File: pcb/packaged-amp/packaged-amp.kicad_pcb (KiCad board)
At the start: 4 copper layers, 70 x 86 mm, 105 parts, among them J2 RFShield_TwoPieces, J7 Conn_Coaxial, J8 USB_B, Q1 MMBT3906, Q2 MMBT3904, U1 TLV2172, U2 OPA2822, U3 LMR62014XMF, U4 L78L06_SOT89, U5 L79L05_SOT89

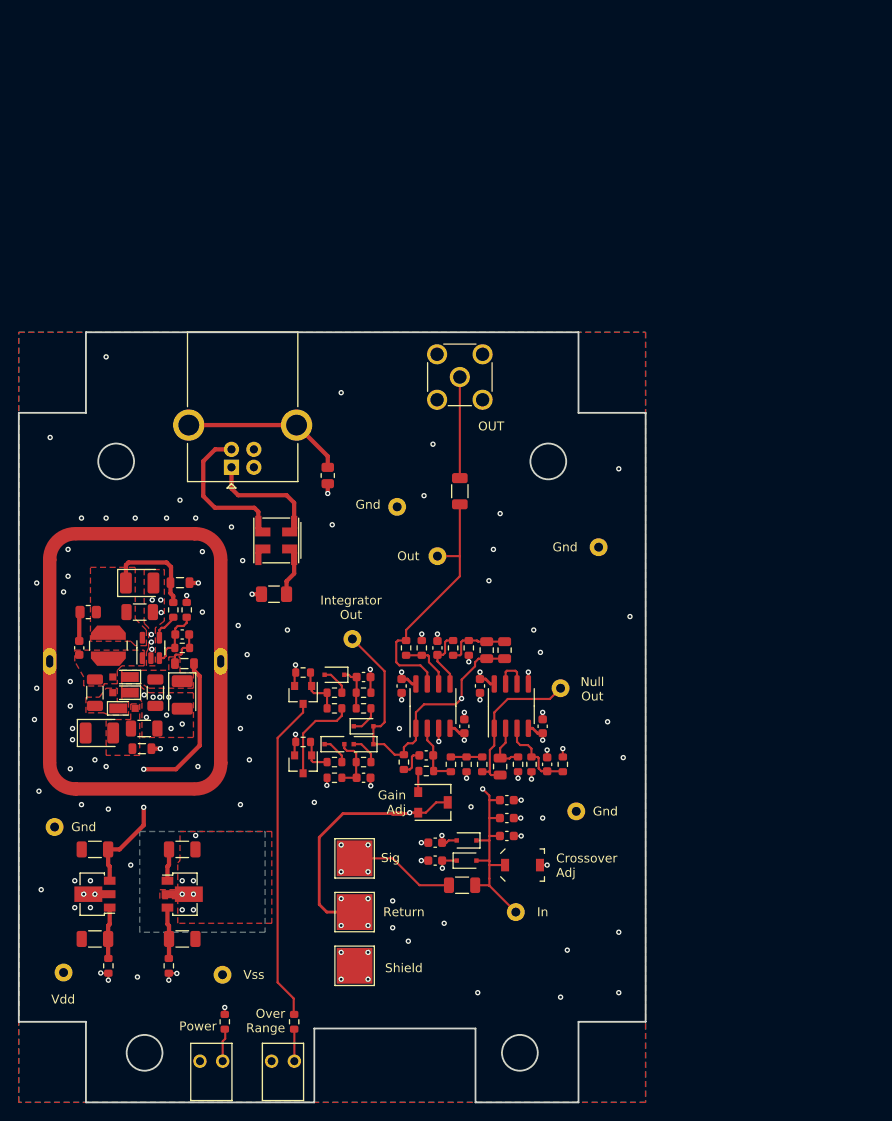
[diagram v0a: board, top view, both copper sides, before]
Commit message: finished design of packaged amp
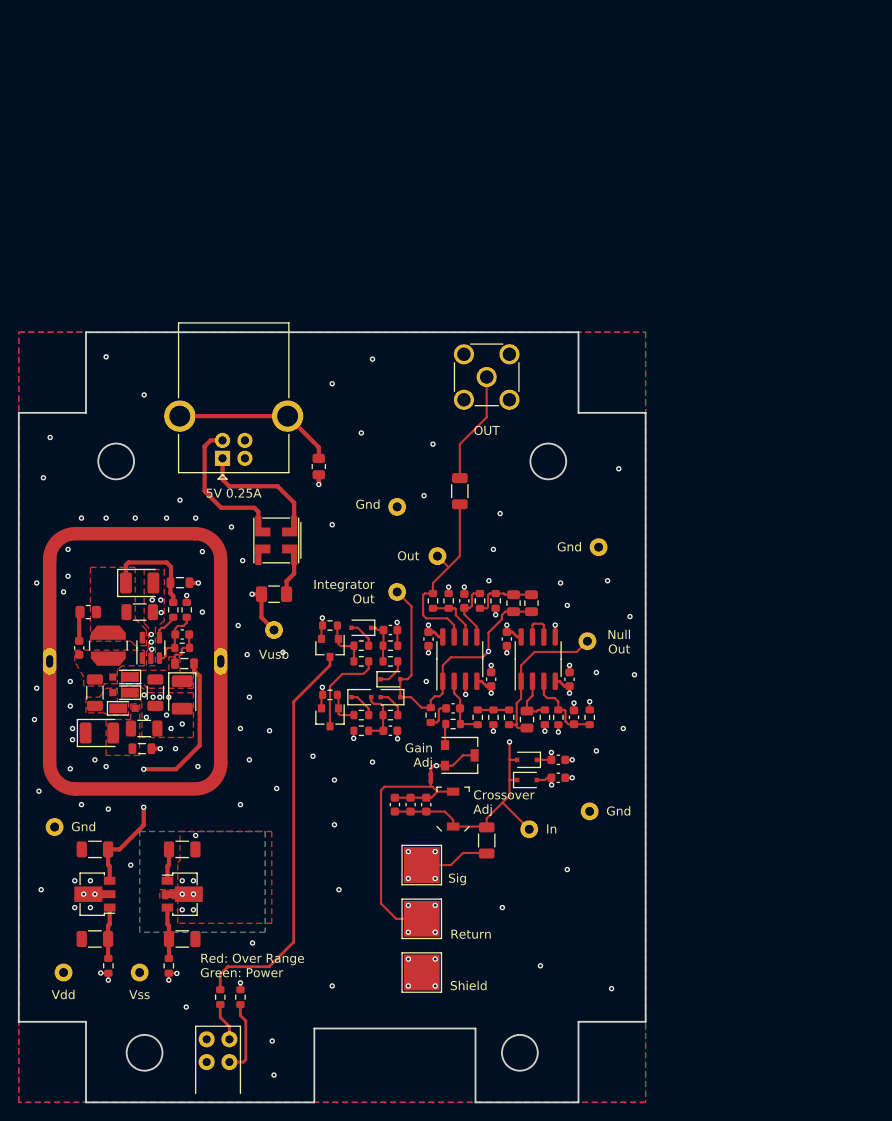
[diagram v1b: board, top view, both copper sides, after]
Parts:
- removed D11: LED, wbraun_smd:LED-T1-RIGHT-ANGLE_4.6x4.4mm
- added TP14: TestPoint, wbraun_smd:THM_MINI, F.Cu at (66.0, 129.8)
- D10: value LED -> LED_Dual_KAKA; footprint wbraun_smd:LED-T1-RIGHT-ANGLE_4.6x4.4mm -> wbraun_smd:LED_WP934MD
- moved C7 17.8 mm to (97.8, 144.2)
- moved C8 15.5 mm to (97.8, 146.2), turned to 180 degrees
- moved D1 13.1 mm to (94.2, 144.2), turned to 180 degrees
- moved C1 13.0 mm to (79.5, 149.2), turned to 90 degrees
- moved C10 10.9 mm to (81.2, 149.2), turned to 90 degrees
- moved C11 9.96 mm to (86.0, 149.8), turned to 90 degrees
- moved D2 9.55 mm to (94.2, 146.5), turned to 0 degrees
- moved TP1 9.37 mm to (94.5, 152.0)
- moved TP10 9.25 mm to (51.0, 168.0)
- moved C9 9.01 mm to (83.0, 149.2), turned to 90 degrees
- moved R28 8.70 mm to (60.0, 170.8)
- moved TP11 7.54 mm to (82.5, 156.0)
- moved TP12 7.54 mm to (82.5, 162.0)
- moved TP13 7.54 mm to (82.5, 168.0)
- moved D10 7.25 mm to (59.8, 178.0), turned to 0 degrees
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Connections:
- C1 pad 2: GND -> /return_kelvin
- C10 pad 2: GND -> /return_kelvin
- C11 pad 2: GND -> /return_kelvin
- C7 pad 1: VDD -> GND
- C7 pad 2: GND -> VDD
- C9 pad 2: GND -> /return_kelvin
- NT1 pad 1: Net-(NT1-Pad1) -> /return_kelvin
- R30 pad 2: Net-(D11-Pad1) -> Net-(R30-Pad2)
- TP12 pad 1: Net-(NT1-Pad1) -> /return_kelvin
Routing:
- net /return_kelvin: track 0.00 -> 31.9 mm, vias 0 -> 4
- net Net-(NT1-Pad1): track 21.1 -> 0.00 mm, vias 4 -> 0
- net Net-(R30-Pad2): track 0.00 -> 8.36 mm
- net Net-(Q2-Pad3): track 36.6 -> 44.9 mm
- net Net-(R12-Pad1): track 28.9 -> 21.6 mm
- net Net-(F1-Pad2): track 8.57 -> 13.2 mm
- net Net-(R1-Pad1): track 11.8 -> 7.84 mm
- net Net-(D11-Pad1): track 3.71 -> 0.00 mm
- net Net-(C1-Pad1): track 34.3 -> 37.1 mm
- net GND: track 25.7 -> 23.0 mm, vias 111 -> 117
- net Net-(J8-Pad1): track 12.2 -> 13.6 mm
- net Net-(J7-Pad1): track 11.3 -> 12.5 mm
- net /int_out: track 50.7 -> 49.8 mm
- net Net-(R28-Pad2): track 3.58 -> 4.31 mm
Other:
- board text added: "5V 0.25A"
- board text added: "Red: Over Range Green: Power"
- board text added: "Vusb"
- board text removed: "Over Range"
- board text removed: "Power"

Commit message: design sent to fab
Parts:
- added D11: SMAJ6.0A-13-F, Diode_SMD:D_SMA, F.Cu at (65.5, 131.0)
- added E1: SparkGap, wbraun_smd:Spark_Gap, F.Cu at (91.2, 154.0)
- added E2: SparkGap, wbraun_smd:Spark_Gap, F.Cu at (73.2, 147.8)
- added GD1: GDT_2Pin, wbraun_smd:GDT_1812, F.Cu at (92.2, 119.5)
- added NT2: NetTie_2, NetTie:NetTie-2_SMD_Pad0.5mm, F.Cu at (89.2, 169.0)
- moved TP14 10.0 mm to (65.2, 139.8)
- moved TP6 6.71 mm to (104.2, 144.0)
- moved R1 3.26 mm to (89.5, 150.0)
- moved TP11 2.50 mm to (80.5, 157.5)
- moved TP12 2.50 mm to (80.5, 163.5)
- moved TP13 2.50 mm to (80.5, 169.5)
- moved TP1 2.37 mm to (95.2, 149.8)
- moved J8 1.00 mm to (60.2, 109.6)
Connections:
- TP13 pad 1: GND -> Net-(NT2-Pad1)
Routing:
- net /return_kelvin: track 31.9 -> 45.7 mm
- net Net-(D11-Pad1): track 13.2 -> 26.6 mm
- net Net-(NT2-Pad1): track 0.00 -> 13.1 mm, vias 0 -> 4
- net Net-(E1-Pad2): track 7.84 -> 20.3 mm
- net Net-(GD1-Pad1): track 21.6 -> 28.2 mm
- net Net-(J8-Pad5): track 18.2 -> 20.7 mm
- net GND: track 23.0 -> 25.0 mm, vias 117 -> 132
- net Net-(J8-Pad4): track 15.4 -> 16.4 mm
- net Net-(J8-Pad1): track 13.6 -> 14.6 mm
- net Net-(C1-Pad1): track 37.1 -> 38.1 mm
- net Net-(Q2-Pad3): track 44.9 -> 45.8 mm
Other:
- outline, holes or cut-outs redrawn
- board text added: "Designed to fit hammond 1593BBBK enclosure"
- board text added: "JLCJLCJLCJLC"
- board text added: "Rogowski Coil Amplifier V1.0"
- board text removed: "OUT"

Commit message: next design revision
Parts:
- removed C18: 47n, Capacitor_SMD:C_0805_2012Metric
- removed C24, C26, C32: 47u, Capacitor_Tantalum_SMD:CP_EIA-3528-15_AVX-H
- removed C33, C34: C, Capacitor_SMD:C_0603_1608Metric
- removed C8: 0.47u, Capacitor_SMD:C_0603_1608Metric
- removed D10: LED_Dual_KAKA, wbraun_smd:LED_WP934MD
- removed D7: 1N4148, Diode_SMD:D_SOD-323F
- removed D8, D9: MM3Z7V5B, Diode_SMD:D_SOD-323F
- removed NT2: NetTie_2, NetTie:NetTie-2_SMD_Pad0.5mm
- removed Q1: MMBT3906, wbraun_smd:SOT-23
- removed Q2: MMBT3904, wbraun_smd:SOT-23
- removed R22, R23, R27: 47k, Resistor_SMD:R_0603_1608Metric
- removed R24, R29: 22k, Resistor_SMD:R_0603_1608Metric
- removed R26: 1M, Resistor_SMD:R_0603_1608Metric
- removed R28, R30: 4.7k, Resistor_SMD:R_0603_1608Metric
- removed R31, R32: 0, Resistor_SMD:R_0603_1608Metric
- removed TP1, TP10, TP2, TP3, TP5, TP7, TP8, TP9: TestPoint, wbraun_smd:THM_MINI
- removed TP13: TestPoint, TestPoint:TestPoint_Pad_4.0x4.0mm
- added C2: 10u, Capacitor_SMD:C_1206_3216Metric, F.Cu at (92.2, 105.0)
- added C3: 10u, Capacitor_SMD:C_1206_3216Metric, F.Cu at (83.8, 109.5)
- added C4: DNP, Capacitor_SMD:C_0603_1608Metric, F.Cu at (112.5, 98.8)
- added G***: LOGO, wbraun_smd:Beefield_logo, F.Cu at (97.8, 159.2)
- added J1: ECT81800C036, wbraun_smd:Shield_Clip_ECT81800C036, F.Cu at (88.0, 90.5)
- added J3: ECT81800C036, wbraun_smd:Shield_Clip_ECT81800C036, F.Cu at (88.0, 115.5)
- added J4: ECT81800C036, wbraun_smd:Shield_Clip_ECT81800C036, F.Cu at (98.0, 103.0)
- C10: value 22p -> DNP
- C11: value 8-40p -> 12-60p; footprint Capacitor_SMD:C_Trimmer_Voltronics_JZ -> wbraun_smd:C_Trimmer_GKG_6mm
- C15: footprint Capacitor_SMD:C_0805_2012Metric -> Capacitor_SMD:C_1206_3216Metric
- C17: value 47n -> DNP; footprint Capacitor_SMD:C_0805_2012Metric -> Capacitor_SMD:C_0603_1608Metric
- C19: value 22p -> 10p
- C22: value 470p -> 330p
- C7: value 0.47u -> 10u; footprint Capacitor_SMD:C_0603_1608Metric -> Capacitor_SMD:C_1206_3216Metric
- C9: value 150p -> 100p
- D11: value SMAJ6.0A-13-F -> P6SMB6.8CA/TR13; footprint Diode_SMD:D_SMA -> Diode_SMD:D_SMB
- D3, D4, D5: value PD3S140-7 -> BAT760-7; footprint wbraun_smd:D_POWERDI323 -> Diode_SMD:D_SOD-323
- D6: value 1N4148 -> LTST-S220KGKT; footprint Diode_SMD:D_SOD-323F -> wbraun_smd:LED-T1-RIGHT-ANGLE_4.6x4.4mm
- J2: value RFShield_TwoPieces -> ECT81800C036; footprint wbraun_smd:Masach_Tech_MS288-10F -> wbraun_smd:Shield_Clip_ECT81800C036
- L2: value L_Ferrite_Coupled -> DLW5BTM142SQ2L
- R1: footprint Resistor_SMD:R_1206_3216Metric -> Resistor_SMD:R_0603_1608Metric
- R10: value 220 -> 470
- R11, R12: value 2k -> 470
- R13: value 47 -> 100
- R15, R18: value 75k -> 82k
- R16: value 13.3k -> 13k
- R19: value R -> DNP
- R2: value 4.7k -> 22k
- R20: value 2k -> DNP
- R21: value 2k -> 100; footprint Resistor_SMD:R_0603_1608Metric -> Resistor_SMD:R_1206_3216Metric
- R25: value 1M -> 4.7k
- R3: value 10k -> 8.2k
- R4, R7: value 47k -> 22k
- R6: value 22k -> DNP
- R8: value 2k -> 10k
- R9: value 10k -> 2k
- RV1: footprint wbraun_smd:TRIMMER_PVG3A -> Potentiometer_SMD:Potentiometer_Bourns_3314G_Vertical
- U4: value L78L06_SOT89 -> MC78L06F-TP
- U5: value L79L05_SOT89 -> MC79L06F-TP
- moved TP4 112.7 mm to (126.2, 77.5)
- moved R20 63.4 mm to (114.5, 86.8), turned to 90 degrees
- moved TP14 62.3 mm to (79.2, 79.0)
- moved R21 60.8 mm to (110.5, 81.2), turned to -90 degrees
- moved C11 57.8 mm to (124.0, 106.2), turned to 180 degrees
- moved D2 56.6 mm to (125.8, 99.5)
- moved D1 56.4 mm to (125.8, 97.5)
- moved C30 56.3 mm to (87.8, 126.5)
- moved U4 55.3 mm to (87.5, 122.8)
- moved C15 54.9 mm to (105.2, 86.0)
- moved C28 54.6 mm to (87.8, 119.0)
- moved C16 54.0 mm to (111.0, 86.8), turned to -90 degrees
- moved R8 54.0 mm to (112.8, 86.8), turned to 90 degrees
- moved R4 53.9 mm to (103.2, 86.8)
- moved C31 53.7 mm to (94.0, 126.5)
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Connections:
- net Net-(C14-Pad1) renamed /int_fb
- C16 pad 1: Net-(C16-Pad1) -> GND
- C16 pad 2: GND -> Net-(C16-Pad2)
- C17 pad 1: /int_out -> /out
- C30 pad 1: Net-(C30-Pad1) -> VDD
- C31 pad 2: Net-(C31-Pad2) -> VSS
- C7 pad 1: GND -> /VBUS
- C7 pad 2: VDD -> GND
- D6 pad 1: /int_out -> VSS
- J7 pad 1: Net-(J7-Pad1) -> Net-(GD1-Pad1)
- R10 pad 2: Net-(C17-Pad2) -> /int_out
- R12 pad 1: Net-(GD1-Pad1) -> /out
- R13 pad 1: Net-(J7-Pad1) -> Net-(GD1-Pad1)
- R13 pad 2: Net-(GD1-Pad1) -> /out
- R20 pad 1: Net-(D6-Pad2) -> Net-(C17-Pad2)
- R20 pad 2: Net-(C33-Pad1) -> GND
- R21 pad 1: Net-(D7-Pad1) -> Net-(GD1-Pad1)
- R21 pad 2: Net-(C34-Pad1) -> /out
- R25 pad 1: Net-(Q1-Pad1) -> Net-(D6-Pad2)
- R6 pad 1: Net-(C15-Pad2) -> Net-(C4-Pad2)
- R7 pad 1: Net-(C16-Pad1) -> Net-(C15-Pad2)
- R7 pad 2: /int_out -> GND
- R8 pad 1: GND -> Net-(C16-Pad2)
- R8 pad 2: Net-(C16-Pad1) -> /out
- R9 pad 2: Net-(C17-Pad2) -> Net-(C16-Pad2)
- RV1 pad 1: Net-(R5-Pad1) -> GND
- RV1 pad 3: GND -> Net-(R5-Pad1)
- U1 pad 1: Net-(C15-Pad1) -> Net-(U1-Pad1)
- U1 pad 2: Net-(C15-Pad2) -> Net-(U1-Pad1)
- U1 pad 3: Net-(C16-Pad1) -> GND
- U1 pad 5: GND -> Net-(C16-Pad2)
- U1 pad 6: Net-(U1-Pad6) -> Net-(C15-Pad2)
- U1 pad 7: Net-(U1-Pad6) -> Net-(C15-Pad1)
- U2 pad 7: Net-(GD1-Pad1) -> /out
- U4 pad 1: Net-(C30-Pad1) -> VDD
- U5 pad 3: Net-(C31-Pad2) -> VSS
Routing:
- net Net-(Q2-Pad3): track 45.8 -> 0.00 mm
- net /int_out: track 49.8 -> 14.6 mm, vias 2 -> 0
- net Net-(R2-Pad2): track 3.50 -> 33.0 mm, vias 0 -> 2
- net /out: track 0.00 -> 16.8 mm
- net VSS: track 15.2 -> 30.7 mm, vias 8 -> 4
- net Net-(NT2-Pad1): track 13.1 -> 0.00 mm, vias 4 -> 0
- net Net-(E1-Pad2): track 20.3 -> 33.1 mm
- net Net-(J8-Pad4): track 16.4 -> 29.0 mm
- net Net-(J7-Pad1): track 12.5 -> 0.00 mm
- net Net-(J8-Pad1): track 14.6 -> 27.0 mm
- net Net-(C15-Pad1): track 17.7 -> 5.74 mm
- net Net-(Q1-Pad3): track 10.4 -> 0.00 mm
- net /return_kelvin: track 45.7 -> 56.1 mm
- net Net-(C16-Pad1): track 9.22 -> 0.00 mm
- net Net-(D10-Pad3): track 8.36 -> 0.00 mm
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- added copper zone on B.Cu, net GND
- added copper zone on In2.Cu, net GND
- added copper zone on In2.Cu, net VDD
- removed copper zone on B.Cu, net VDD
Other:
- board size 70 x 86 mm -> 56.6 x 82.7 mm
- board text removed: "5V 0.25A"
- board text removed: "Crossover Adj"
- board text removed: "Designed to fit hammond 1593BBBK enclosure"
- board text removed: "Gain Adj"
- board text removed: "In"
- board text removed: "Integrator Out"
- board text removed: "Null Out"
- board text removed: "Out"
- board text removed: "Red: Over Range Green: Power"
- board text removed: "Return"
- board text removed: "Shield"
- board text removed: "Sig"
- board text removed: "Vdd"
- board text removed: "Vss"
- board text removed: "Vusb"

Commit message: design revision
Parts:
- removed FB5: FerriteBead_Small, Inductor_SMD:L_0805_2012Metric
- removed G***: LOGO, wbraun_smd:Beefield_logo
- removed R19: DNP, Resistor_SMD:R_0805_2012Metric
- removed R20: DNP, Resistor_SMD:R_0603_1608Metric
- removed R21: 100, Resistor_SMD:R_1206_3216Metric
- removed TP14: TestPoint, wbraun_smd:THM_MINI
- added C18: 0.47u, Capacitor_SMD:C_0603_1608Metric, F.Cu at (84.8, 79.5)
- added C24: 10u, Capacitor_SMD:C_1206_3216Metric, F.Cu at (89.2, 85.2)
- added C8: 0.47u, Capacitor_SMD:C_0603_1608Metric, F.Cu at (84.8, 71.0)
- added H1: MountingHole, wbraun_smd:beefield_logo_small, F.Cu at (125.2, 141.6)
- added L3: 6.8u, Inductor_SMD:L_1210_3225Metric, F.Cu at (86.0, 85.2)
- added U6: B0505S-1WR3, wbraun_smd:Converter_DCDC_1W_Isolated_Short, F.Cu at (77.6, 71.0)
- C17: value DNP -> 1n; footprint Capacitor_SMD:C_0603_1608Metric -> Capacitor_SMD:C_1206_3216Metric
- C4: value DNP -> 10u; footprint Capacitor_SMD:C_0603_1608Metric -> Capacitor_SMD:C_1206_3216Metric
- D6: value LTST-S220KGKT -> WP934CB/GD
- L2: value DLW5BTM142SQ2L -> 6.8u; footprint wbraun_smd:L_CommonModeChoke_Murata_DLW5BTM -> Inductor_SMD:L_1210_3225Metric
- R13: value 100 -> 47
- R6: value DNP -> 47
- moved C4 43.1 mm to (84.2, 66.2), turned to 0 degrees
- moved C17 33.1 mm to (85.2, 75.2)
- moved TP6 22.5 mm to (129.2, 119.0)
- moved D11 17.0 mm to (89.0, 68.2), turned to 90 degrees
- moved TP4 15.2 mm to (114.0, 68.5)
- moved R6 14.5 mm to (125.2, 98.8)
- moved GD1 14.1 mm to (125.8, 76.5), turned to 0 degrees
- moved R13 10.8 mm to (123.5, 81.5)
- moved F1 7.91 mm to (89.0, 73.2), turned to 180 degrees
- moved L2 7.62 mm to (79.5, 66.2), turned to 180 degrees
- moved R25 6.77 mm to (84.0, 130.8), turned to 0 degrees
- moved D6 5.11 mm to (84.5, 136.9)
- moved C1 2.25 mm to (115.0, 107.8)
- moved C10 2.25 mm to (116.8, 107.8)
- moved C11 2.25 mm to (126.2, 106.2)
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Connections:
- C17 pad 1: /out -> /USB_GND
- C17 pad 2: Net-(C17-Pad2) -> GND
- C4 pad 1: /int_out -> /USB_PWR
- C4 pad 2: Net-(C4-Pad2) -> /USB_GND
- D11 pad 1: Net-(D11-Pad1) -> /USB_PWR
- D11 pad 2: GND -> /USB_GND
- F1 pad 2: Net-(D11-Pad1) -> /USB_PWR
- J8 pad 1: Net-(J8-Pad1) -> Net-(F1-Pad1)
- J8 pad 4: Net-(J8-Pad4) -> /USB_GND
- J8 pad 5: Net-(J8-Pad5) -> /USB_GND
- L2 pad 1: Net-(J8-Pad1) -> /USB_PWR
- L2 pad 2: Net-(F1-Pad1) -> Net-(C8-Pad1)
- R6 pad 1: Net-(C4-Pad2) -> Net-(C1-Pad1)
- R6 pad 2: GND -> Net-(R6-Pad2)
- U2 pad 3: Net-(C1-Pad1) -> Net-(R6-Pad2)
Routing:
- net Net-(J8-Pad4): track 29.0 -> 0.00 mm
- net Net-(J8-Pad1): track 27.0 -> 0.00 mm
- net Net-(D11-Pad1): track 21.6 -> 0.00 mm, vias 2 -> 0
- net Net-(J8-Pad5): track 15.7 -> 0.00 mm
- net /USB_PWR: track 0.00 -> 14.9 mm
- net Net-(C8-Pad1): track 0.00 -> 14.8 mm
- net Net-(C18-Pad1): track 0.00 -> 11.9 mm
- net Net-(GD1-Pad1): track 21.7 -> 11.4 mm
- net /VBUS: track 8.97 -> 16.9 mm, vias 0 -> 2
- net Net-(F1-Pad1): track 3.05 -> 10.3 mm
- net /USB_GND: track 0.00 -> 7.08 mm, vias 0 -> 6
- net VSS: track 30.7 -> 23.7 mm
- net Net-(R6-Pad2): track 0.00 -> 6.59 mm
- net Net-(C1-Pad1): track 33.9 -> 27.8 mm
- net VDD: track 20.2 -> 15.6 mm
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- added copper zone on B.Cu, net /USB_GND
- added copper zone on In1.Cu, net /USB_GND
- added copper zone on In2.Cu, net /USB_PWR
- added copper zone on F.Cu, net Net-(C8-Pad1)
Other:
- outline, holes or cut-outs redrawn
- board text added: "Beefield Labs"
- board text added: "Generic clip in 25x20mm rf sheild"
- board text added: "Ret"
- board text added: "Rogowski Coil Amplifier V2.0 2022"
- board text added: "Sig"
- board text added: "Use with PLP5-2-125 light pipe (3.2mm deep)"
- board text added: "github.com/westonb/rogowski-relief"
- board text removed: "Gnd"
- board text removed: "Rogowski Coil Amplifier V1.0"

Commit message: pcb sent to production
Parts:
- removed C20, C23, C24, C25, C27: 10u, Capacitor_SMD:C_1206_3216Metric
- removed C21: DNP, Capacitor_SMD:C_0603_1608Metric
- removed C22: 330p, Capacitor_SMD:C_0603_1608Metric
- removed D3, D4, D5: BAT760-7, Diode_SMD:D_SOD-323
- removed FB3, FB4: FerriteBead_Small, Inductor_SMD:L_0805_2012Metric
- removed J1, J2, J3, J4: ECT81800C036, wbraun_smd:Shield_Clip_ECT81800C036
- removed R15, R18: 82k, Resistor_SMD:R_0603_1608Metric
- removed R16: 13k, Resistor_SMD:R_0603_1608Metric
- removed R17: DNP, Resistor_SMD:R_0805_2012Metric
- removed U3: LMR62014XMF, Package_TO_SOT_SMD:SOT-23-5
- removed U6: B0505S-1WR3, wbraun_smd:Converter_DCDC_1W_Isolated_Short
- added FB1: FerriteBead_Small, Inductor_SMD:L_0805_2012Metric, F.Cu at (92.2, 114.2)
- added FB2: FerriteBead_Small, Inductor_SMD:L_0805_2012Metric, F.Cu at (96.2, 104.8)
- added H2: MountingHole, wbraun_smd:JLC_TOOLING_HOLE, F.Cu at (78.9, 143.7)
- added H3: MountingHole, wbraun_smd:JLC_TOOLING_HOLE, F.Cu at (78.9, 67.0)
- added H4: MountingHole, wbraun_smd:JLC_TOOLING_HOLE, F.Cu at (129.5, 132.2)
- added H5: MountingHole, wbraun_smd:JLC_TOOLING_HOLE, F.Cu at (130.5, 66.0)
- added L4: 10u, Inductor_SMD:L_1210_3225Metric, F.Cu at (90.5, 104.8)
- added PS1: A0509S-2WR3, Converter_DCDC:Converter_DCDC_XP_POWER-IHxxxxS_THT, F.Cu at (82.8, 95.3)
- C18, C8: value 0.47u -> 10u; footprint Capacitor_SMD:C_0603_1608Metric -> Capacitor_SMD:C_1206_3216Metric
- L1: value 10u -> DLW5BTM102SQ2L; footprint wbraun_smd:L_VLCF4020 -> wbraun_smd:L_CommonModeChoke_Murata_DLW5BTM
- L2, L3: value 6.8u -> 10u
- NT1: value NetTie_2 -> DNP
- R3: value 8.2k -> 22k
- R5: value 365 -> 360
- R9: value 2k -> 470
- TP11, TP12, TP4, TP6: value TestPoint -> DNP
- moved C8 40.1 mm to (94.0, 110.0)
- moved C4 30.1 mm to (90.0, 95.8), turned to -90 degrees
- moved L1 28.8 mm to (86.0, 71.0), turned to 180 degrees
- moved C18 27.4 mm to (94.0, 105.2)
- moved L2 26.8 mm to (88.5, 91.5)
- moved L3 25.6 mm to (90.5, 110.5), turned to 0 degrees
- moved C17 25.3 mm to (87.0, 100.5)
- moved D11 18.6 mm to (87.5, 86.8), turned to 180 degrees
- moved C7 12.1 mm to (87.0, 105.2), turned to 90 degrees
- moved C2 10.6 mm to (87.0, 95.8)
- moved F1 9.83 mm to (87.8, 83.0), turned to 0 degrees
- moved C3 3.29 mm to (87.0, 110.0), turned to 90 degrees
- moved D6 1.00 mm to (84.5, 137.9)
- moved C1 0.50 mm to (115.0, 108.2)
- moved C10 0.50 mm to (116.8, 108.2)
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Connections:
- C17 pad 2: GND -> Net-(C17-Pad2)
- C18 pad 1: Net-(C18-Pad1) -> GND
- C18 pad 2: GND -> Net-(C18-Pad2)
- C2 pad 1: /VDD_unreg -> Net-(C2-Pad1)
- C2 pad 2: GND -> /USB_GND
- C28 pad 1: Net-(C28-Pad1) -> /VDD_unreg
- C29 pad 2: Net-(C29-Pad2) -> /VSS_unreg
- C3 pad 1: GND -> Net-(C3-Pad1)
- C3 pad 2: /VSS_unreg -> GND
- C7 pad 1: /VBUS -> GND
- C7 pad 2: GND -> Net-(C17-Pad2)
- C8 pad 2: /USB_GND -> GND
- J8 pad 1: Net-(F1-Pad1) -> Net-(J8-Pad1)
- J8 pad 4: /USB_GND -> Net-(J8-Pad4)
- J8 pad 5: /USB_GND -> Net-(J8-Pad4)
- L1 pad 1: /VBUS -> Net-(J8-Pad1)
- L1 pad 2: Net-(C21-Pad2) -> Net-(F1-Pad1)
- L2 pad 2: Net-(C8-Pad1) -> Net-(C2-Pad1)
- L3 pad 1: Net-(C18-Pad1) -> Net-(C3-Pad1)
- L3 pad 2: /VBUS -> Net-(C8-Pad1)
- U4 pad 3: Net-(C28-Pad1) -> /VDD_unreg
- U5 pad 2: Net-(C29-Pad2) -> /VSS_unreg
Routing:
- net Net-(J8-Pad4): track 0.00 -> 31.1 mm
- net Net-(C28-Pad1): track 25.9 -> 0.00 mm, vias 2 -> 0
- net /VBUS: track 16.9 -> 0.00 mm, vias 2 -> 0
- net /USB_PWR: track 14.9 -> 0.00 mm, vias 0 -> 4
- net Net-(C8-Pad1): track 14.8 -> 0.00 mm
- net /VSS_unreg: track 2.32 -> 15.1 mm, vias 0 -> 3
- net Net-(C29-Pad2): track 12.6 -> 0.00 mm, vias 5 -> 0
- net Net-(J8-Pad1): track 0.00 -> 11.9 mm
- net Net-(C18-Pad1): track 11.9 -> 0.00 mm
- net /USB_GND: track 7.08 -> 0.00 mm, vias 6 -> 28
- net Net-(C22-Pad1): track 6.93 -> 0.00 mm
- net GND: track 25.7 -> 30.4 mm, vias 94 -> 92
- net Net-(F1-Pad1): track 10.3 -> 14.2 mm
- net /VDD_unreg: track 4.70 -> 8.14 mm
- net Net-(R15-Pad1): track 3.11 -> 0.00 mm
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- added copper zone on F.Cu, net /USB_GND
- added copper zone on F.Cu, net /USB_PWR
- added copper zone on B.Cu, net /VSS_unreg
- added copper zone on F.Cu, net Net-(C17-Pad2)
- added copper zone on F.Cu, net Net-(C18-Pad2)
- added copper zone on F.Cu, net Net-(C2-Pad1)
- added copper zone on F.Cu, net Net-(C3-Pad1)
- removed copper zone on F.Cu, net /VBUS
- removed copper zone on F.Cu, net /VDD_unreg
- removed copper zone on F.Cu, net Net-(C21-Pad2)
- removed copper zone on F.Cu, net Net-(C23-Pad1)
- removed copper zone on B.Cu, net Net-(C29-Pad2)
- removed copper zone on F.Cu, net Net-(C29-Pad2)
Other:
- outline, holes or cut-outs redrawn
- board text added: "5V 0.25A"
- board text removed: "Generic clip in 25x20mm rf sheild"
